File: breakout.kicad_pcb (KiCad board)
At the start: 2 copper layers, 103 x 62 mm, 31 parts, among them CON1 SD_Card, CON2 USB-MICRO-AB, P2 CONN_01X40, P3 CONN_01X40, P4 CONN_01X40, P5 A-DF-09-A/KG-T4S, SW1 SW_PUSH

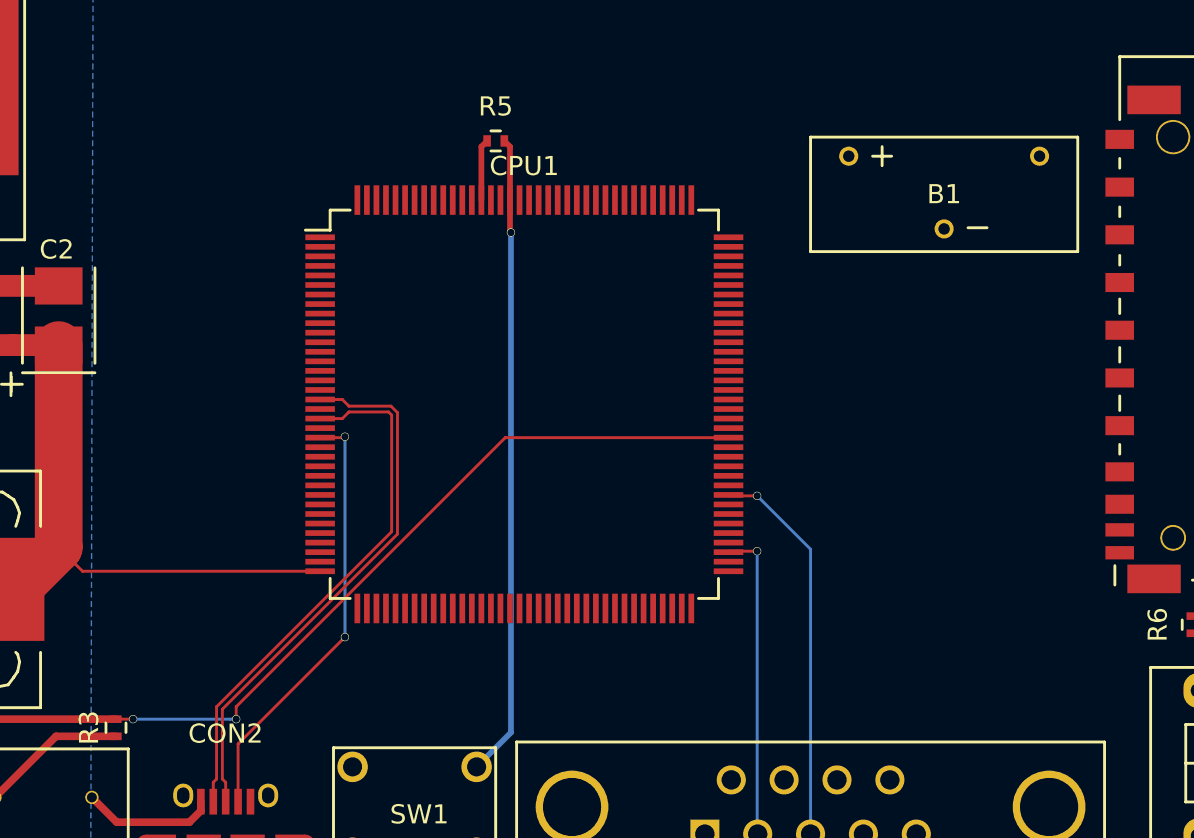
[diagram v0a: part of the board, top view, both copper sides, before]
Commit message: locked components and switched USB0_PPWP to pin 50
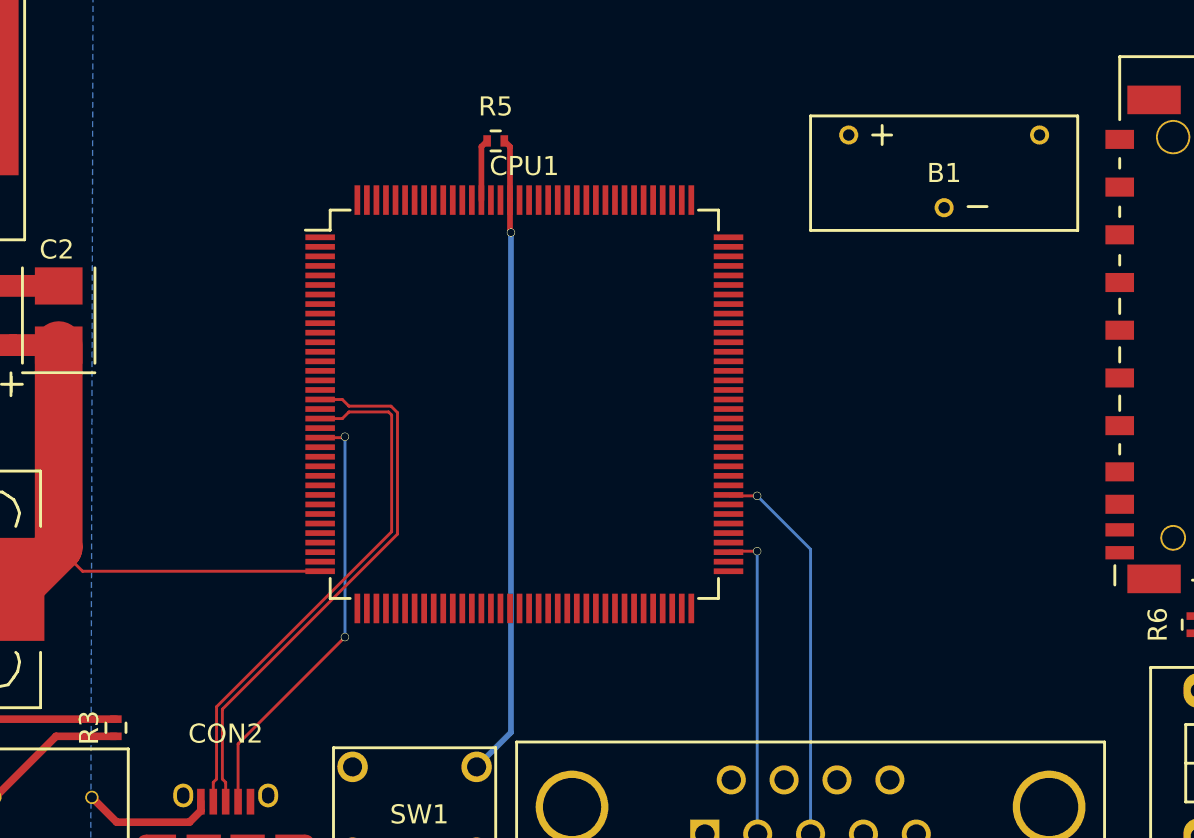
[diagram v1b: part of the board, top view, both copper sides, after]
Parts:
- moved B1 1.11 mm to (132.0, 135.9)
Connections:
- CPU1 pad 1: (no net) -> /P4_0
- CPU1 pad 10: (no net) -> /P4_5
- CPU1 pad 100: (no net) -> /P6_10
- CPU1 pad 101: (no net) -> /P6_11
- CPU1 pad 103: (no net) -> /P6_12
- CPU1 pad 104: (no net) -> /P2_10
- CPU1 pad 105: (no net) -> /P2_11
- CPU1 pad 106: (no net) -> /P2_12
- CPU1 pad 108: (no net) -> /P2_13
- CPU1 pad 11: (no net) -> /P4_6
- CPU1 pad 110: (no net) -> /P7_0
- CPU1 pad 112: (no net) -> /P3_0
- CPU1 pad 113: (no net) -> /P7_1
- CPU1 pad 114: (no net) -> /P3_1
- CPU1 pad 115: (no net) -> /P7_2
- CPU1 pad 116: (no net) -> /P3_2
- CPU1 pad 117: (no net) -> /P7_3
- CPU1 pad 118: (no net) -> /SPI_SCK
- CPU1 pad 119: (no net) -> /P3_4
- CPU1 pad 12: (no net) -> /XTAL1
- CPU1 pad 120: (no net) -> /PF_4
- CPU1 pad 121: (no net) -> /P3_5
- CPU1 pad 122: (no net) -> /SPI_MISO
- CPU1 pad 123: (no net) -> /SPI_MOSI
- CPU1 pad 124: (no net) -> /SPI_SSEL
- CPU1 pad 125: (no net) -> /RTCX1
- CPU1 pad 126: (no net) -> /RTCX2
- CPU1 pad 129: (no net) -> /RTC_ALARM
- CPU1 pad 13: (no net) -> /XTAL2
- CPU1 pad 130: (no net) -> /WAKEUP0
- CPU1 pad 132: (no net) -> /P7_4
- CPU1 pad 133: (no net) -> /P7_5
- CPU1 pad 134: (no net) -> /P7_6
- CPU1 pad 136: (no net) -> /ADC0_7
- CPU1 pad 138: (no net) -> /ADC0_4
- CPU1 pad 139: (no net) -> /ADC0_3
- CPU1 pad 14: (no net) -> /P4_7
- CPU1 pad 140: (no net) -> /P7_7
- CPU1 pad 142: (no net) -> /ADC0_6
- CPU1 pad 143: (no net) -> /ADC0_2
- CPU1 pad 144: (no net) -> /ADC0_5
- CPU1 pad 15: (no net) -> /P4_8
- CPU1 pad 16: (no net) -> Net-(CPU1-Pad16)
- CPU1 pad 17: (no net) -> Net-(CPU1-Pad17)
- CPU1 pad 19: (no net) -> Net-(CPU1-Pad19)
- CPU1 pad 2: (no net) -> /ADC0_1
- CPU1 pad 21: (no net) -> Net-(CPU1-Pad21)
- CPU1 pad 23: (no net) -> Net-(CPU1-Pad23)
- CPU1 pad 24: (no net) -> Net-(CPU1-Pad24)
- CPU1 pad 26: (no net) -> /TDI
- CPU1 pad 27: (no net) -> /TCK
- CPU1 pad 28: (no net) -> /DBGEN
- CPU1 pad 29: (no net) -> /TRST
- CPU1 pad 3: (no net) -> /P4_1
- CPU1 pad 30: (no net) -> /TMS
- CPU1 pad 31: (no net) -> /TDO
- CPU1 pad 33: (no net) -> /P4_9
- CPU1 pad 34: (no net) -> /P0_1
- CPU1 pad 35: (no net) -> /P4_10
- CPU1 pad 37: (no net) -> /P5_0
- CPU1 pad 38: (no net) -> /P1_0
- CPU1 pad 39: (no net) -> /P5_1
- CPU1 pad 44: (no net) -> /P1_3
- CPU1 pad 46: (no net) -> /P5_2
- CPU1 pad 47: (no net) -> /USB0_IND0
- CPU1 pad 48: (no net) -> /P1_5
- CPU1 pad 50: (no net) -> /USB0_PPWR
- CPU1 pad 51: (no net) -> /P1_8
- CPU1 pad 54: (no net) -> /P5_3
- CPU1 pad 57: (no net) -> /P5_4
- CPU1 pad 58: (no net) -> /P5_5
- CPU1 pad 6: (no net) -> /ADC0_0
- CPU1 pad 61: (no net) -> /P1_14
- CPU1 pad 62: (no net) -> /P1_15
- CPU1 pad 63: (no net) -> /P5_6
- CPU1 pad 64: (no net) -> /P1_16
- CPU1 pad 65: (no net) -> /P5_7
- CPU1 pad 66: (no net) -> /P1_17
- CPU1 pad 67: (no net) -> /P1_18
- CPU1 pad 68: (no net) -> /P1_19
- CPU1 pad 69: (no net) -> /P9_5
- CPU1 pad 7: (no net) -> /P4_3
- CPU1 pad 70: (no net) -> /P1_20
- CPU1 pad 72: (no net) -> /P9_6
- CPU1 pad 73: (no net) -> /P6_0
- CPU1 pad 74: (no net) -> /P6_1
- CPU1 pad 78: (no net) -> /P6_2
- CPU1 pad 79: (no net) -> /P6_3
- CPU1 pad 8: (no net) -> /P4_2
- CPU1 pad 80: (no net) -> /P6_4
- CPU1 pad 82: (no net) -> /P6_5
- CPU1 pad 83: (no net) -> /P6_6
- CPU1 pad 84: (no net) -> /P2_2
- CPU1 pad 85: (no net) -> /P6_7
- CPU1 pad 86: (no net) -> /P6_8
- CPU1 pad 87: /USB0_PPWR -> /P2_3
- CPU1 pad 88: (no net) -> /P2_4
- CPU1 pad 89: (no net) -> /USB1_D+
- CPU1 pad 9: (no net) -> /P4_4
- CPU1 pad 90: (no net) -> /USB1_D-
- CPU1 pad 91: (no net) -> /P2_5
- CPU1 pad 92: (no net) -> /I2C0_SCL
- CPU1 pad 93: (no net) -> /I2C0_SDA
- CPU1 pad 95: (no net) -> /P2_6
- CPU1 pad 97: (no net) -> /P6_9
- CPU1 pad 99: (no net) -> /CLK2
- P2 pad 1: (no net) -> Net-(P2-Pad1)
- P2 pad 10: (no net) -> Net-(P2-Pad10)
- P2 pad 11: (no net) -> Net-(P2-Pad11)
- P2 pad 12: (no net) -> Net-(P2-Pad12)
- P2 pad 13: (no net) -> Net-(P2-Pad13)
- P2 pad 14: (no net) -> Net-(P2-Pad14)
- P2 pad 15: (no net) -> Net-(P2-Pad15)
- P2 pad 16: (no net) -> Net-(P2-Pad16)
- P2 pad 17: (no net) -> Net-(P2-Pad17)
- P2 pad 18: (no net) -> Net-(P2-Pad18)
- P2 pad 19: (no net) -> Net-(P2-Pad19)
- P2 pad 2: (no net) -> Net-(P2-Pad2)
- P2 pad 20: (no net) -> Net-(P2-Pad20)
- P2 pad 21: (no net) -> Net-(P2-Pad21)
- P2 pad 22: (no net) -> Net-(P2-Pad22)
- P2 pad 23: (no net) -> Net-(P2-Pad23)
- P2 pad 24: (no net) -> Net-(P2-Pad24)
- P2 pad 25: (no net) -> Net-(P2-Pad25)
- P2 pad 26: (no net) -> Net-(P2-Pad26)
- P2 pad 27: (no net) -> Net-(P2-Pad27)
- P2 pad 28: (no net) -> Net-(P2-Pad28)
- P2 pad 29: (no net) -> Net-(P2-Pad29)
- P2 pad 3: (no net) -> Net-(P2-Pad3)
- P2 pad 30: (no net) -> Net-(P2-Pad30)
- P2 pad 31: (no net) -> Net-(P2-Pad31)
- P2 pad 32: (no net) -> Net-(P2-Pad32)
- P2 pad 33: (no net) -> Net-(P2-Pad33)
- P2 pad 34: (no net) -> Net-(P2-Pad34)
- P2 pad 35: (no net) -> Net-(P2-Pad35)
- P2 pad 36: (no net) -> Net-(P2-Pad36)
- P2 pad 37: (no net) -> Net-(P2-Pad37)
- P2 pad 38: (no net) -> Net-(P2-Pad38)
- P2 pad 39: (no net) -> Net-(P2-Pad39)
- P2 pad 4: (no net) -> Net-(P2-Pad4)
- P2 pad 40: (no net) -> Net-(P2-Pad40)
- P2 pad 5: (no net) -> Net-(P2-Pad5)
- P2 pad 6: (no net) -> Net-(P2-Pad6)
- P2 pad 7: (no net) -> Net-(P2-Pad7)
- P2 pad 8: (no net) -> Net-(P2-Pad8)
- P2 pad 9: (no net) -> Net-(P2-Pad9)
- P3 pad 1: (no net) -> Net-(P3-Pad1)
- P3 pad 10: (no net) -> Net-(P3-Pad10)
- P3 pad 11: (no net) -> Net-(P3-Pad11)
- P3 pad 12: (no net) -> Net-(P3-Pad12)
- P3 pad 13: (no net) -> Net-(P3-Pad13)
- P3 pad 14: (no net) -> Net-(P3-Pad14)
- P3 pad 15: (no net) -> Net-(P3-Pad15)
- P3 pad 16: (no net) -> Net-(P3-Pad16)
- P3 pad 17: (no net) -> Net-(P3-Pad17)
- P3 pad 18: (no net) -> Net-(P3-Pad18)
- P3 pad 19: (no net) -> Net-(P3-Pad19)
- P3 pad 2: (no net) -> Net-(P3-Pad2)
- P3 pad 20: (no net) -> Net-(P3-Pad20)
- P3 pad 21: (no net) -> Net-(P3-Pad21)
- P3 pad 22: (no net) -> Net-(P3-Pad22)
- P3 pad 23: (no net) -> Net-(P3-Pad23)
- P3 pad 24: (no net) -> Net-(P3-Pad24)
- P3 pad 25: (no net) -> Net-(P3-Pad25)
- P3 pad 26: (no net) -> Net-(P3-Pad26)
- P3 pad 27: (no net) -> Net-(P3-Pad27)
- P3 pad 28: (no net) -> Net-(P3-Pad28)
- P3 pad 29: (no net) -> Net-(P3-Pad29)
- P3 pad 3: (no net) -> Net-(P3-Pad3)
- P3 pad 30: (no net) -> Net-(P3-Pad30)
- P3 pad 31: (no net) -> Net-(P3-Pad31)
- P3 pad 32: (no net) -> Net-(P3-Pad32)
- P3 pad 33: (no net) -> Net-(P3-Pad33)
- P3 pad 34: (no net) -> Net-(P3-Pad34)
- P3 pad 35: (no net) -> Net-(P3-Pad35)
- P3 pad 36: (no net) -> Net-(P3-Pad36)
- P3 pad 37: (no net) -> Net-(P3-Pad37)
- P3 pad 38: (no net) -> Net-(P3-Pad38)
- P3 pad 39: (no net) -> Net-(P3-Pad39)
- P3 pad 4: (no net) -> Net-(P3-Pad4)
- P3 pad 40: (no net) -> Net-(P3-Pad40)
- P3 pad 5: (no net) -> Net-(P3-Pad5)
- P3 pad 6: (no net) -> Net-(P3-Pad6)
- P3 pad 7: (no net) -> Net-(P3-Pad7)
- P3 pad 8: (no net) -> Net-(P3-Pad8)
- P3 pad 9: (no net) -> Net-(P3-Pad9)
- P4 pad 1: (no net) -> Net-(P4-Pad1)
- P4 pad 10: (no net) -> Net-(P4-Pad10)
- P4 pad 11: (no net) -> Net-(P4-Pad11)
- P4 pad 12: (no net) -> Net-(P4-Pad12)
- P4 pad 13: (no net) -> Net-(P4-Pad13)
- P4 pad 14: (no net) -> Net-(P4-Pad14)
- P4 pad 15: (no net) -> Net-(P4-Pad15)
- P4 pad 16: (no net) -> Net-(P4-Pad16)
- P4 pad 17: (no net) -> Net-(P4-Pad17)
- P4 pad 18: (no net) -> Net-(P4-Pad18)
- P4 pad 19: (no net) -> Net-(P4-Pad19)
- P4 pad 2: (no net) -> Net-(P4-Pad2)
- P4 pad 20: (no net) -> Net-(P4-Pad20)
- P4 pad 21: (no net) -> Net-(P4-Pad21)
- P4 pad 22: (no net) -> Net-(P4-Pad22)
- P4 pad 23: (no net) -> Net-(P4-Pad23)
- P4 pad 24: (no net) -> Net-(P4-Pad24)
- P4 pad 25: (no net) -> Net-(P4-Pad25)
- P4 pad 26: (no net) -> Net-(P4-Pad26)
- P4 pad 27: (no net) -> Net-(P4-Pad27)
- P4 pad 28: (no net) -> Net-(P4-Pad28)
- P4 pad 29: (no net) -> Net-(P4-Pad29)
- P4 pad 3: (no net) -> Net-(P4-Pad3)
- P4 pad 30: (no net) -> Net-(P4-Pad30)
- P4 pad 31: (no net) -> Net-(P4-Pad31)
- P4 pad 32: (no net) -> Net-(P4-Pad32)
- P4 pad 33: (no net) -> Net-(P4-Pad33)
- P4 pad 34: (no net) -> Net-(P4-Pad34)
- P4 pad 35: (no net) -> Net-(P4-Pad35)
- P4 pad 36: (no net) -> Net-(P4-Pad36)
- P4 pad 37: (no net) -> Net-(P4-Pad37)
- P4 pad 38: (no net) -> Net-(P4-Pad38)
- P4 pad 39: (no net) -> Net-(P4-Pad39)
- P4 pad 4: (no net) -> Net-(P4-Pad4)
- P4 pad 40: (no net) -> Net-(P4-Pad40)
- P4 pad 5: (no net) -> Net-(P4-Pad5)
- P4 pad 6: (no net) -> Net-(P4-Pad6)
- P4 pad 7: (no net) -> Net-(P4-Pad7)
- P4 pad 8: (no net) -> Net-(P4-Pad8)
- P4 pad 9: (no net) -> Net-(P4-Pad9)
- P5 pad 1: (no net) -> Net-(P5-Pad1)
- P5 pad 4: (no net) -> Net-(P5-Pad4)
- P5 pad 6: (no net) -> Net-(P5-Pad6)
- P5 pad 7: (no net) -> Net-(P5-Pad7)
- P5 pad 8: (no net) -> Net-(P5-Pad8)
- P5 pad 9: (no net) -> Net-(P5-Pad9)
- PWR2 pad 6: (no net) -> Net-(PWR2-Pad6)
- PWR2 pad 7: (no net) -> Net-(PWR2-Pad7)
- PWR2 pad 9: (no net) -> Net-(PWR2-Pad9)
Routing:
- net /USB0_PPWR: track 51.7 -> 13.1 mm, vias 2 -> 0

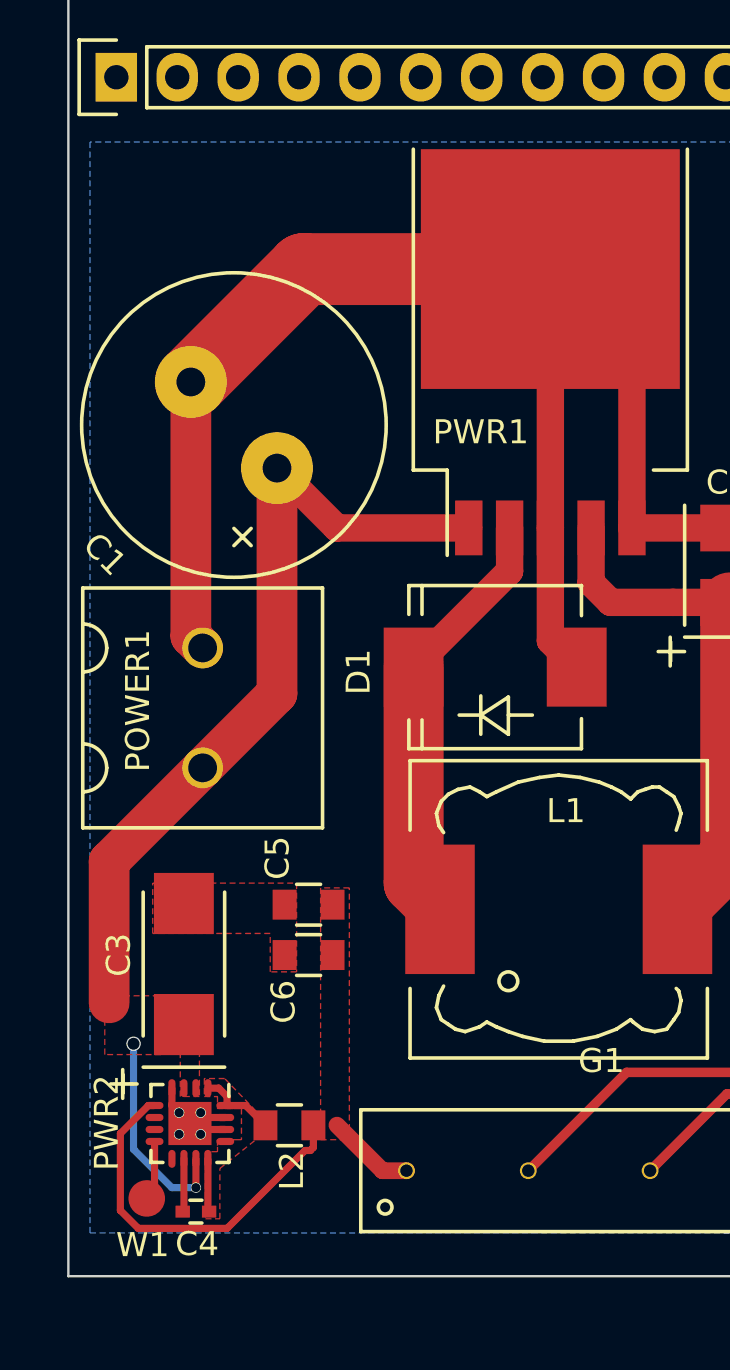
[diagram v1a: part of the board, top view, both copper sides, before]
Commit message: added polarity protection D2, and locked components
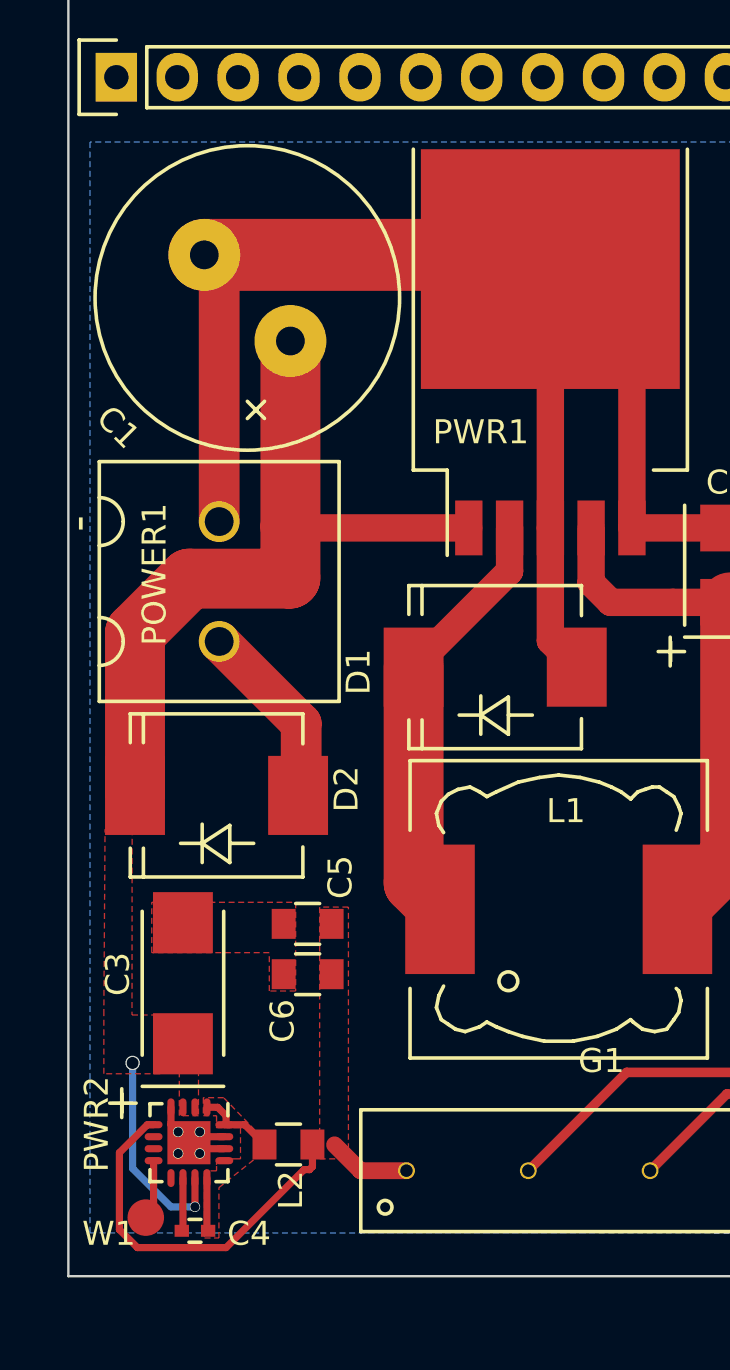
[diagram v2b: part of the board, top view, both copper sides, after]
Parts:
- added D2: B340, Diodes_SMD:Diode-SMC_Standard, F.Cu at (64.2, 154.9)
- moved C1 5.33 mm to (67.3, 136.0)
- moved POWER1 5.31 mm to (64.3, 143.5)
- moved PWR2 0.80 mm to (63.0, 169.4)
- moved W1 0.80 mm to (61.2, 172.6)
- moved C5 0.80 mm to (68.0, 160.3)
- moved C6 0.80 mm to (68.0, 162.4)
- moved C3 0.80 mm to (62.8, 162.8)
- moved C4 0.80 mm to (63.3, 173.1)
- moved L2 0.80 mm to (67.2, 169.5)
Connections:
- CPU1 pad 1: /P4_0 -> (no net)
- CPU1 pad 10: /P4_5 -> (no net)
- CPU1 pad 100: /P6_10 -> (no net)
- CPU1 pad 101: /P6_11 -> (no net)
- CPU1 pad 103: /P6_12 -> (no net)
- CPU1 pad 104: /P2_10 -> (no net)
- CPU1 pad 105: /P2_11 -> (no net)
- CPU1 pad 106: /P2_12 -> (no net)
- CPU1 pad 108: /P2_13 -> (no net)
- CPU1 pad 11: /P4_6 -> (no net)
- CPU1 pad 110: /P7_0 -> (no net)
- CPU1 pad 112: /P3_0 -> (no net)
- CPU1 pad 113: /P7_1 -> (no net)
- CPU1 pad 114: /P3_1 -> (no net)
- CPU1 pad 115: /P7_2 -> (no net)
- CPU1 pad 116: /P3_2 -> (no net)
- CPU1 pad 117: /P7_3 -> (no net)
- CPU1 pad 118: /SPI_SCK -> (no net)
- CPU1 pad 119: /P3_4 -> (no net)
- CPU1 pad 12: /XTAL1 -> (no net)
- CPU1 pad 120: /PF_4 -> (no net)
- CPU1 pad 121: /P3_5 -> (no net)
- CPU1 pad 122: /SPI_MISO -> (no net)
- CPU1 pad 123: /SPI_MOSI -> (no net)
- CPU1 pad 124: /SPI_SSEL -> (no net)
- CPU1 pad 125: /RTCX1 -> (no net)
- CPU1 pad 126: /RTCX2 -> (no net)
- CPU1 pad 129: /RTC_ALARM -> (no net)
- CPU1 pad 13: /XTAL2 -> (no net)
- CPU1 pad 130: /WAKEUP0 -> (no net)
- CPU1 pad 132: /P7_4 -> (no net)
- CPU1 pad 133: /P7_5 -> (no net)
- CPU1 pad 134: /P7_6 -> (no net)
- CPU1 pad 136: /ADC0_7 -> (no net)
- CPU1 pad 138: /ADC0_4 -> (no net)
- CPU1 pad 139: /ADC0_3 -> (no net)
- CPU1 pad 14: /P4_7 -> (no net)
- CPU1 pad 140: /P7_7 -> (no net)
- CPU1 pad 142: /ADC0_6 -> (no net)
- CPU1 pad 143: /ADC0_2 -> (no net)
- CPU1 pad 144: /ADC0_5 -> (no net)
- CPU1 pad 15: /P4_8 -> (no net)
- CPU1 pad 16: Net-(CPU1-Pad16) -> (no net)
- CPU1 pad 17: Net-(CPU1-Pad17) -> (no net)
- CPU1 pad 19: Net-(CPU1-Pad19) -> (no net)
- CPU1 pad 2: /ADC0_1 -> (no net)
- CPU1 pad 21: Net-(CPU1-Pad21) -> (no net)
- CPU1 pad 23: Net-(CPU1-Pad23) -> (no net)
- CPU1 pad 24: Net-(CPU1-Pad24) -> (no net)
- CPU1 pad 26: /TDI -> (no net)
- CPU1 pad 27: /TCK -> (no net)
- CPU1 pad 28: /DBGEN -> (no net)
- CPU1 pad 29: /TRST -> (no net)
- CPU1 pad 3: /P4_1 -> (no net)
- CPU1 pad 30: /TMS -> (no net)
- CPU1 pad 31: /TDO -> (no net)
- CPU1 pad 33: /P4_9 -> (no net)
- CPU1 pad 34: /P0_1 -> (no net)
- CPU1 pad 35: /P4_10 -> (no net)
- CPU1 pad 37: /P5_0 -> (no net)
- CPU1 pad 38: /P1_0 -> (no net)
- CPU1 pad 39: /P5_1 -> (no net)
- CPU1 pad 44: /P1_3 -> (no net)
- CPU1 pad 46: /P5_2 -> (no net)
- CPU1 pad 47: /USB0_IND0 -> (no net)
- CPU1 pad 48: /P1_5 -> (no net)
- CPU1 pad 51: /P1_8 -> (no net)
- CPU1 pad 54: /P5_3 -> (no net)
- CPU1 pad 57: /P5_4 -> (no net)
- CPU1 pad 58: /P5_5 -> (no net)
- CPU1 pad 6: /ADC0_0 -> (no net)
- CPU1 pad 61: /P1_14 -> (no net)
- CPU1 pad 62: /P1_15 -> (no net)
- CPU1 pad 63: /P5_6 -> (no net)
- CPU1 pad 64: /P1_16 -> (no net)
- CPU1 pad 65: /P5_7 -> (no net)
- CPU1 pad 66: /P1_17 -> (no net)
- CPU1 pad 67: /P1_18 -> (no net)
- CPU1 pad 68: /P1_19 -> (no net)
- CPU1 pad 69: /P9_5 -> (no net)
- CPU1 pad 7: /P4_3 -> (no net)
- CPU1 pad 70: /P1_20 -> (no net)
- CPU1 pad 72: /P9_6 -> (no net)
- CPU1 pad 73: /P6_0 -> (no net)
- CPU1 pad 74: /P6_1 -> (no net)
- CPU1 pad 78: /P6_2 -> (no net)
- CPU1 pad 79: /P6_3 -> (no net)
- CPU1 pad 8: /P4_2 -> (no net)
- CPU1 pad 80: /P6_4 -> (no net)
- CPU1 pad 82: /P6_5 -> (no net)
- CPU1 pad 83: /P6_6 -> (no net)
- CPU1 pad 84: /P2_2 -> (no net)
- CPU1 pad 85: /P6_7 -> (no net)
- CPU1 pad 86: /P6_8 -> (no net)
- CPU1 pad 87: /P2_3 -> (no net)
- CPU1 pad 88: /P2_4 -> (no net)
- CPU1 pad 89: /USB1_D+ -> (no net)
- CPU1 pad 9: /P4_4 -> (no net)
- CPU1 pad 90: /USB1_D- -> (no net)
- CPU1 pad 91: /P2_5 -> (no net)
- CPU1 pad 92: /I2C0_SCL -> (no net)
- CPU1 pad 93: /I2C0_SDA -> (no net)
- CPU1 pad 95: /P2_6 -> (no net)
- CPU1 pad 97: /P6_9 -> (no net)
- CPU1 pad 99: /CLK2 -> (no net)
- P2 pad 1: Net-(P2-Pad1) -> (no net)
- P2 pad 10: Net-(P2-Pad10) -> (no net)
- P2 pad 11: Net-(P2-Pad11) -> (no net)
- P2 pad 12: Net-(P2-Pad12) -> (no net)
- P2 pad 13: Net-(P2-Pad13) -> (no net)
- P2 pad 14: Net-(P2-Pad14) -> (no net)
- P2 pad 15: Net-(P2-Pad15) -> (no net)
- P2 pad 16: Net-(P2-Pad16) -> (no net)
- P2 pad 17: Net-(P2-Pad17) -> (no net)
- P2 pad 18: Net-(P2-Pad18) -> (no net)
- P2 pad 19: Net-(P2-Pad19) -> (no net)
- P2 pad 2: Net-(P2-Pad2) -> (no net)
- P2 pad 20: Net-(P2-Pad20) -> (no net)
- P2 pad 21: Net-(P2-Pad21) -> (no net)
- P2 pad 22: Net-(P2-Pad22) -> (no net)
- P2 pad 23: Net-(P2-Pad23) -> (no net)
- P2 pad 24: Net-(P2-Pad24) -> (no net)
- P2 pad 25: Net-(P2-Pad25) -> (no net)
- P2 pad 26: Net-(P2-Pad26) -> (no net)
- P2 pad 27: Net-(P2-Pad27) -> (no net)
- P2 pad 28: Net-(P2-Pad28) -> (no net)
- P2 pad 29: Net-(P2-Pad29) -> (no net)
- P2 pad 3: Net-(P2-Pad3) -> (no net)
- P2 pad 30: Net-(P2-Pad30) -> (no net)
- P2 pad 31: Net-(P2-Pad31) -> (no net)
- P2 pad 32: Net-(P2-Pad32) -> (no net)
- P2 pad 33: Net-(P2-Pad33) -> (no net)
- P2 pad 34: Net-(P2-Pad34) -> (no net)
- P2 pad 35: Net-(P2-Pad35) -> (no net)
- P2 pad 36: Net-(P2-Pad36) -> (no net)
- P2 pad 37: Net-(P2-Pad37) -> (no net)
- P2 pad 38: Net-(P2-Pad38) -> (no net)
- P2 pad 39: Net-(P2-Pad39) -> (no net)
- P2 pad 4: Net-(P2-Pad4) -> (no net)
- P2 pad 40: Net-(P2-Pad40) -> (no net)
- P2 pad 5: Net-(P2-Pad5) -> (no net)
- P2 pad 6: Net-(P2-Pad6) -> (no net)
- P2 pad 7: Net-(P2-Pad7) -> (no net)
- P2 pad 8: Net-(P2-Pad8) -> (no net)
- P2 pad 9: Net-(P2-Pad9) -> (no net)
- P3 pad 1: Net-(P3-Pad1) -> (no net)
- P3 pad 10: Net-(P3-Pad10) -> (no net)
- P3 pad 11: Net-(P3-Pad11) -> (no net)
- P3 pad 12: Net-(P3-Pad12) -> (no net)
- P3 pad 13: Net-(P3-Pad13) -> (no net)
- P3 pad 14: Net-(P3-Pad14) -> (no net)
- P3 pad 15: Net-(P3-Pad15) -> (no net)
- P3 pad 16: Net-(P3-Pad16) -> (no net)
- P3 pad 17: Net-(P3-Pad17) -> (no net)
- P3 pad 18: Net-(P3-Pad18) -> (no net)
- P3 pad 19: Net-(P3-Pad19) -> (no net)
- P3 pad 2: Net-(P3-Pad2) -> (no net)
- P3 pad 20: Net-(P3-Pad20) -> (no net)
- P3 pad 21: Net-(P3-Pad21) -> (no net)
- P3 pad 22: Net-(P3-Pad22) -> (no net)
- P3 pad 23: Net-(P3-Pad23) -> (no net)
- P3 pad 24: Net-(P3-Pad24) -> (no net)
- P3 pad 25: Net-(P3-Pad25) -> (no net)
- P3 pad 26: Net-(P3-Pad26) -> (no net)
- P3 pad 27: Net-(P3-Pad27) -> (no net)
- P3 pad 28: Net-(P3-Pad28) -> (no net)
- P3 pad 29: Net-(P3-Pad29) -> (no net)
- P3 pad 3: Net-(P3-Pad3) -> (no net)
- P3 pad 30: Net-(P3-Pad30) -> (no net)
- P3 pad 31: Net-(P3-Pad31) -> (no net)
- P3 pad 32: Net-(P3-Pad32) -> (no net)
- P3 pad 33: Net-(P3-Pad33) -> (no net)
- P3 pad 34: Net-(P3-Pad34) -> (no net)
- P3 pad 35: Net-(P3-Pad35) -> (no net)
- P3 pad 36: Net-(P3-Pad36) -> (no net)
- P3 pad 37: Net-(P3-Pad37) -> (no net)
- P3 pad 38: Net-(P3-Pad38) -> (no net)
- P3 pad 39: Net-(P3-Pad39) -> (no net)
- P3 pad 4: Net-(P3-Pad4) -> (no net)
- P3 pad 40: Net-(P3-Pad40) -> (no net)
- P3 pad 5: Net-(P3-Pad5) -> (no net)
- P3 pad 6: Net-(P3-Pad6) -> (no net)
- P3 pad 7: Net-(P3-Pad7) -> (no net)
- P3 pad 8: Net-(P3-Pad8) -> (no net)
- P3 pad 9: Net-(P3-Pad9) -> (no net)
- P4 pad 1: Net-(P4-Pad1) -> (no net)
- P4 pad 10: Net-(P4-Pad10) -> (no net)
- P4 pad 11: Net-(P4-Pad11) -> (no net)
- P4 pad 12: Net-(P4-Pad12) -> (no net)
- P4 pad 13: Net-(P4-Pad13) -> (no net)
- P4 pad 14: Net-(P4-Pad14) -> (no net)
- P4 pad 15: Net-(P4-Pad15) -> (no net)
- P4 pad 16: Net-(P4-Pad16) -> (no net)
- P4 pad 17: Net-(P4-Pad17) -> (no net)
- P4 pad 18: Net-(P4-Pad18) -> (no net)
- P4 pad 19: Net-(P4-Pad19) -> (no net)
- P4 pad 2: Net-(P4-Pad2) -> (no net)
- P4 pad 20: Net-(P4-Pad20) -> (no net)
- P4 pad 21: Net-(P4-Pad21) -> (no net)
- P4 pad 22: Net-(P4-Pad22) -> (no net)
- P4 pad 23: Net-(P4-Pad23) -> (no net)
- P4 pad 24: Net-(P4-Pad24) -> (no net)
- P4 pad 25: Net-(P4-Pad25) -> (no net)
- P4 pad 26: Net-(P4-Pad26) -> (no net)
- P4 pad 27: Net-(P4-Pad27) -> (no net)
- P4 pad 28: Net-(P4-Pad28) -> (no net)
- P4 pad 29: Net-(P4-Pad29) -> (no net)
- P4 pad 3: Net-(P4-Pad3) -> (no net)
- P4 pad 30: Net-(P4-Pad30) -> (no net)
- P4 pad 31: Net-(P4-Pad31) -> (no net)
- P4 pad 32: Net-(P4-Pad32) -> (no net)
- P4 pad 33: Net-(P4-Pad33) -> (no net)
- P4 pad 34: Net-(P4-Pad34) -> (no net)
- P4 pad 35: Net-(P4-Pad35) -> (no net)
- P4 pad 36: Net-(P4-Pad36) -> (no net)
- P4 pad 37: Net-(P4-Pad37) -> (no net)
- P4 pad 38: Net-(P4-Pad38) -> (no net)
- P4 pad 39: Net-(P4-Pad39) -> (no net)
- P4 pad 4: Net-(P4-Pad4) -> (no net)
- P4 pad 40: Net-(P4-Pad40) -> (no net)
- P4 pad 5: Net-(P4-Pad5) -> (no net)
- P4 pad 6: Net-(P4-Pad6) -> (no net)
- P4 pad 7: Net-(P4-Pad7) -> (no net)
- P4 pad 8: Net-(P4-Pad8) -> (no net)
- P4 pad 9: Net-(P4-Pad9) -> (no net)
- P5 pad 1: Net-(P5-Pad1) -> (no net)
- P5 pad 4: Net-(P5-Pad4) -> (no net)
- P5 pad 6: Net-(P5-Pad6) -> (no net)
- P5 pad 7: Net-(P5-Pad7) -> (no net)
- P5 pad 8: Net-(P5-Pad8) -> (no net)
- P5 pad 9: Net-(P5-Pad9) -> (no net)
- POWER1 pad 2: /RAIL -> Net-(D2-Pad1)
- PWR2 pad 6: Net-(PWR2-Pad6) -> (no net)
- PWR2 pad 7: Net-(PWR2-Pad7) -> (no net)
- PWR2 pad 9: Net-(PWR2-Pad9) -> (no net)
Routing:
- net Net-(D2-Pad1): track 0.00 -> 7.89 mm
- net /RAIL: track 43.1 -> 40.4 mm
- net GND: track 72.6 -> 70.4 mm
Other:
- board text added: "-"
